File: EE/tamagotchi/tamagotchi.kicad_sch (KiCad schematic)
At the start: 0 parts

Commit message: Generic Continutation Checkin
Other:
- sheet Display ports: added GREEN_EN, RED_EN, VAPE_EN, YELLOW_EN; removed none
- sheet Power ports: added CE_N, INT_N, SCL, SDA, VSYS; removed none
- sheet Vape ports: added VAPE_EN; removed none
- note added: "TODO can 3v3 be done?"
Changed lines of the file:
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@@
 	(generator_version "9.0")
 	(paper "A4")
+	(text "TODO can 3v3 be done?"
+		(exclude_from_sim no)
+		(at 106.934 81.28 90)
+		(effects
+			(font
+				(size 1.27 1.27)
+			)
+		)
+	)
+	(wire
+		(pts
+			(xy 97.79 91.44) (xy 102.87 91.44)
+		)
+		(stroke
+			(width 0)
+			(type default)
+		)
+	)
+	(wire
+		(pts
+			(xy 102.87 91.44) (xy 102.87 87.63)
+		)
+		(stroke
+			(width 0)
+			(type default)
+		)
+	)
+	(symbol
+		(lib_id "power:+3V3")
+		(at 102.87 87.63 0)
+		(unit 1)
+		(exclude_from_sim no)
+		(in_bom yes)
+		(on_board yes)
+		(dnp no)
+		(fields_autoplaced yes)
+		(property "Reference" "#PWR09"
+			(at 102.87 91.44 0)
+			(effects
+				(font
+					(size 1.27 1.27)
+				)
+				(hide yes)
+			)
+		)
+		(property "Value" "+3V3"
+			(at 102.87 82.55 0)
+			(effects
+				(font
+					(size 1.27 1.27)
+				)
+			)
+		)
+		(property "Footprint" ""
+			(at 102.87 87.63 0)
+			(effects
+				(font
+					(size 1.27 1.27)
+				)
+				(hide yes)
+			)
+		)
+		(property "Datasheet" ""
+			(at 102.87 87.63 0)
+			(effects
+				(font
+					(size 1.27 1.27)
+				)
+				(hide yes)
+			)
+		)
+		(property "Description" "Power symbol creates a global label with name \"+3V3\""
+			(at 102.87 87.63 0)
+			(effects
+				(font
+					(size 1.27 1.27)
+				)
+				(hide yes)
+			)
+		)
+		(pin "1"
+		)
+		(instances
+			(project ""
+				(path "/47ffaef6-4682-4a87-a393-bad1a10963be"
+					(reference "#PWR09")
+					(unit 1)
+				)
+			)
+		)
+	)
 	(sheet
 		(at 52.07 88.9)
@@
 				)
 				(justify left top)
+			)
+		)
+		(pin "CE_N" input
+			(at 97.79 113.03 0)
+			(effects
+				(font
+					(size 1.27 1.27)
+				)
+				(justify right)
+			)
+		)
+		(pin "INT_N" input
+			(at 97.79 115.57 0)
+			(effects
+				(font
+					(size 1.27 1.27)
+				)
+				(justify right)
+			)
+		)
+		(pin "SCL" input
+			(at 97.79 118.11 0)
+			(effects
+				(font
+					(size 1.27 1.27)
+				)
+				(justify right)
+			)
+		)
+		(pin "SDA" input
+			(at 97.79 120.65 0)
+			(effects
+				(font
+					(size 1.27 1.27)
+				)
+				(justify right)
+			)
+		)
+		(pin "VSYS" input
+			(at 97.79 91.44 0)
+			(effects
+				(font
+					(size 1.27 1.27)
+				)
+				(justify right)
 			)
 		)
@@
 			)
 		)
+		(pin "GREEN_EN" input
+			(at 129.54 135.89 180)
+			(effects
+				(font
+					(size 1.27 1.27)
+				)
+				(justify left)
+			)
+		)
+		(pin "RED_EN" input
+			(at 129.54 138.43 180)
+			(effects
+				(font
+					(size 1.27 1.27)
+				)
+				(justify left)
+			)
+		)
+		(pin "VAPE_EN" input
+			(at 129.54 143.51 180)
+			(effects
+				(font
+					(size 1.27 1.27)
+				)
+				(justify left)
+			)
+		)
+		(pin "YELLOW_EN" input
+			(at 129.54 140.97 180)
+			(effects
+				(font
+					(size 1.27 1.27)
+				)
+				(justify left)
+			)
+		)
 		(instances
 			(project "tamagotchi"
@@
 			)
 		)
+		(pin "VAPE_EN" input
+			(at 181.61 93.98 180)
+			(effects
+				(font
+					(size 1.27 1.27)
+				)
+				(justify left)
+			)
+		)

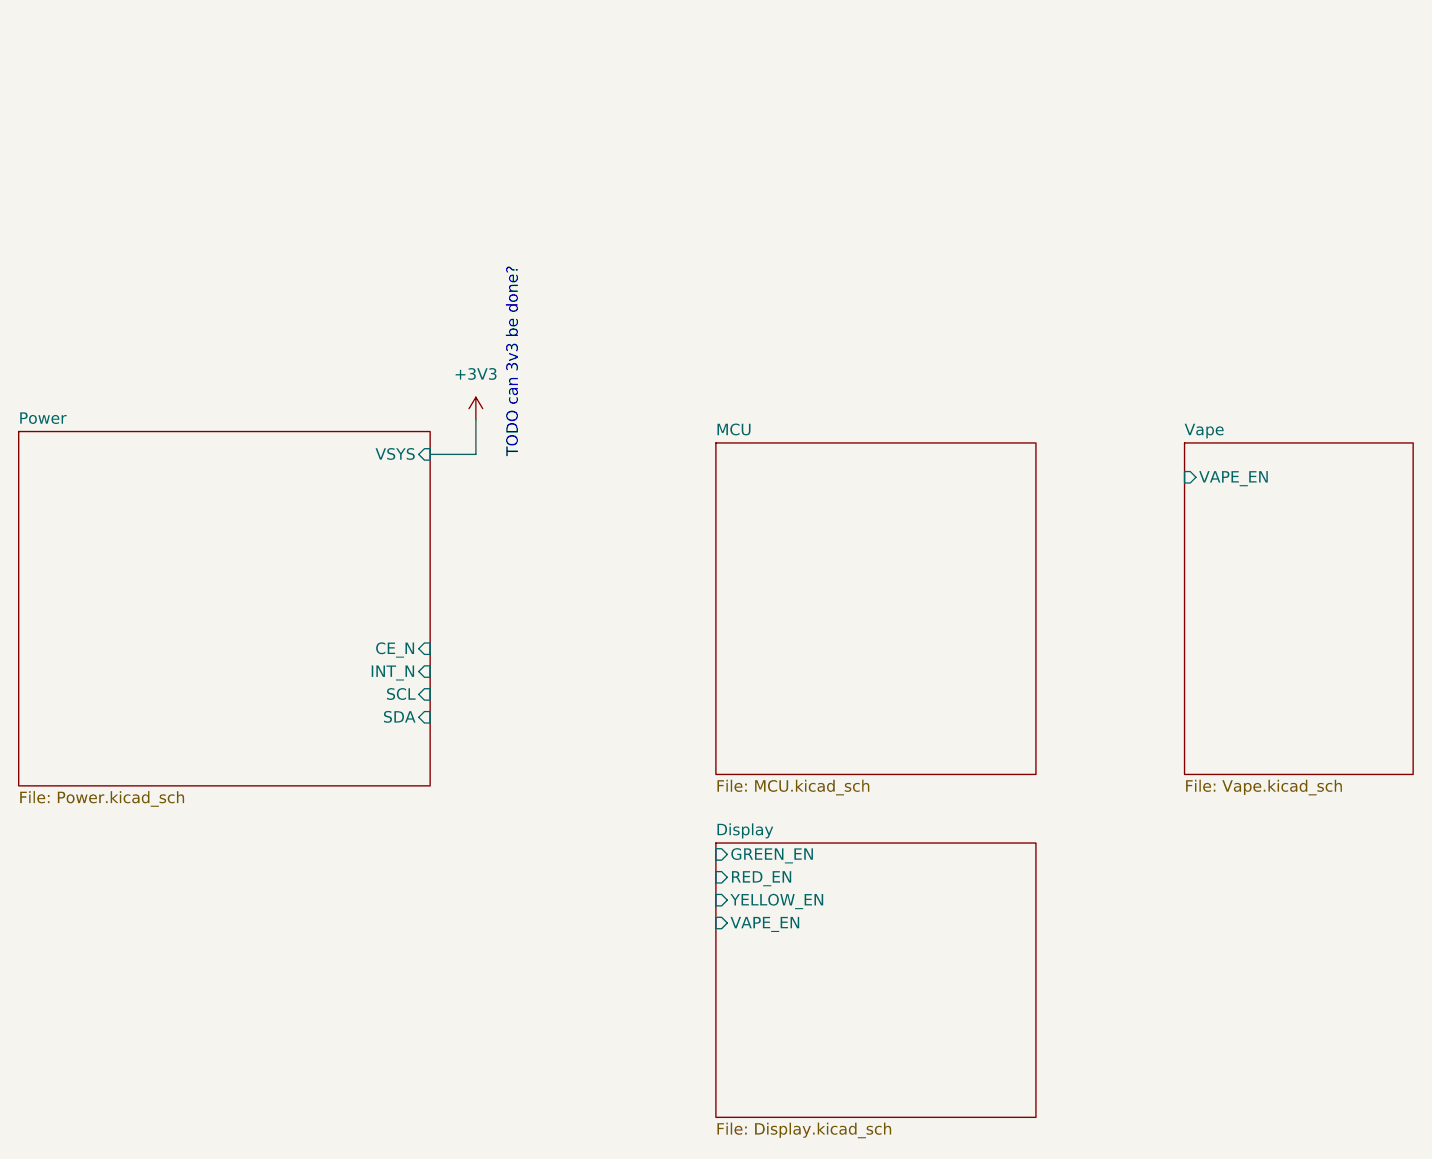
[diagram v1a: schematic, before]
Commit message: WIP - added 3D / footprints for devices. RGY LEDs aren't right
Need to do more outling / ect. super rough placement for everything.
LED footprint for RGY appears just wrong
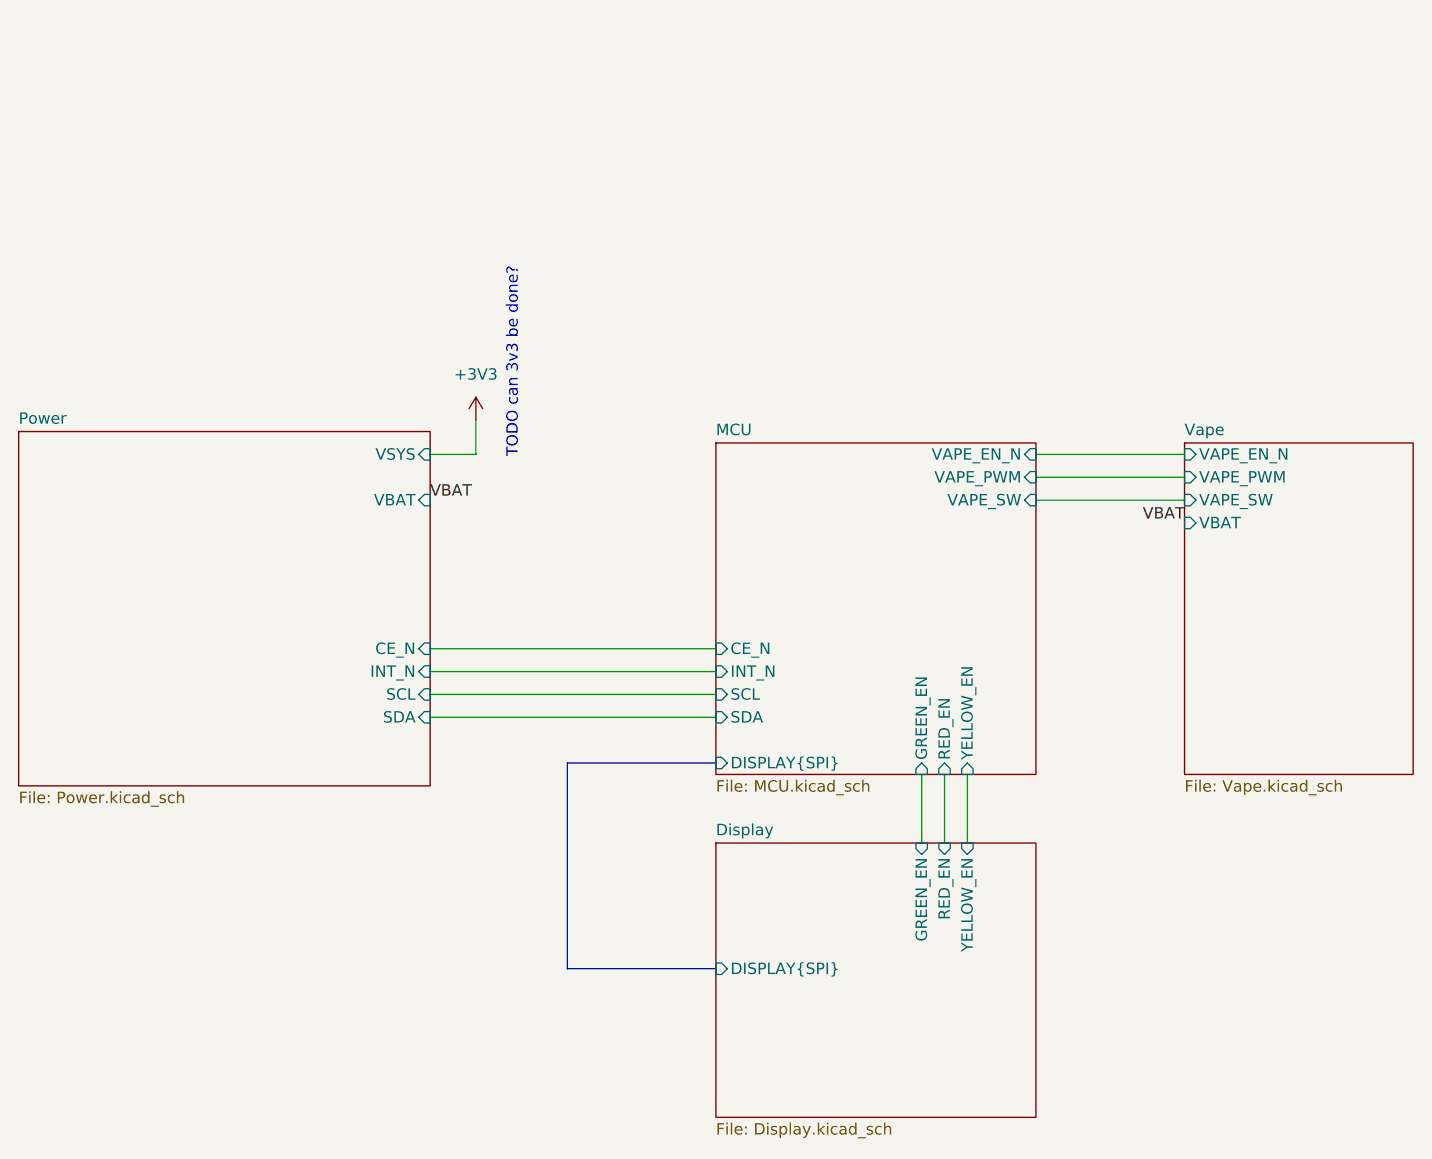
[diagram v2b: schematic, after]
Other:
- sheet Display ports: added DISPLAY{SPI}; removed VAPE_EN
- sheet MCU ports: added CE_N, DISPLAY{SPI}, GREEN_EN, INT_N, RED_EN, SCL, SDA, VAPE_EN_N, VAPE_PWM, VAPE_SW, YELLOW_EN; removed none
- sheet Power ports: added VBAT; removed none
- sheet Vape ports: added VAPE_EN_N, VAPE_PWM, VAPE_SW, VBAT; removed VAPE_EN

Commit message: Removed LEDs
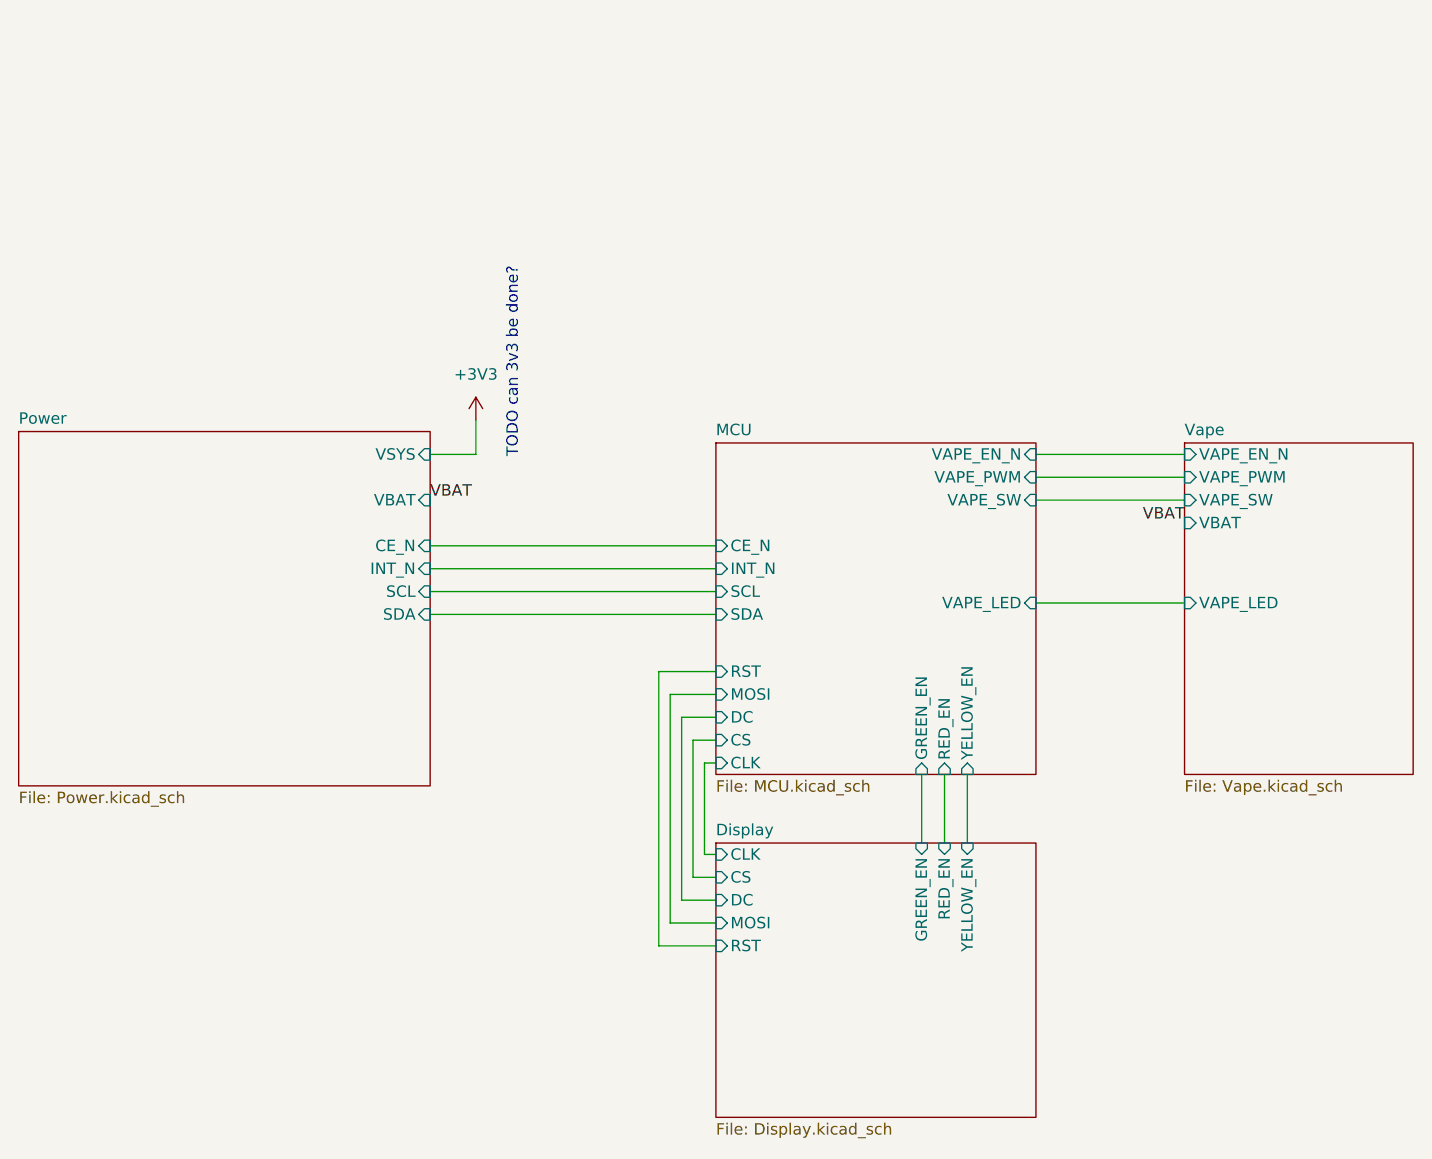
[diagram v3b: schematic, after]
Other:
- sheet Display ports: added CLK, CS, DC, MOSI, RST; removed DISPLAY{SPI}
- sheet MCU ports: added CLK, CS, DC, MOSI, RST, VAPE_LED; removed DISPLAY{SPI}
- sheet Vape ports: added VAPE_LED; removed none

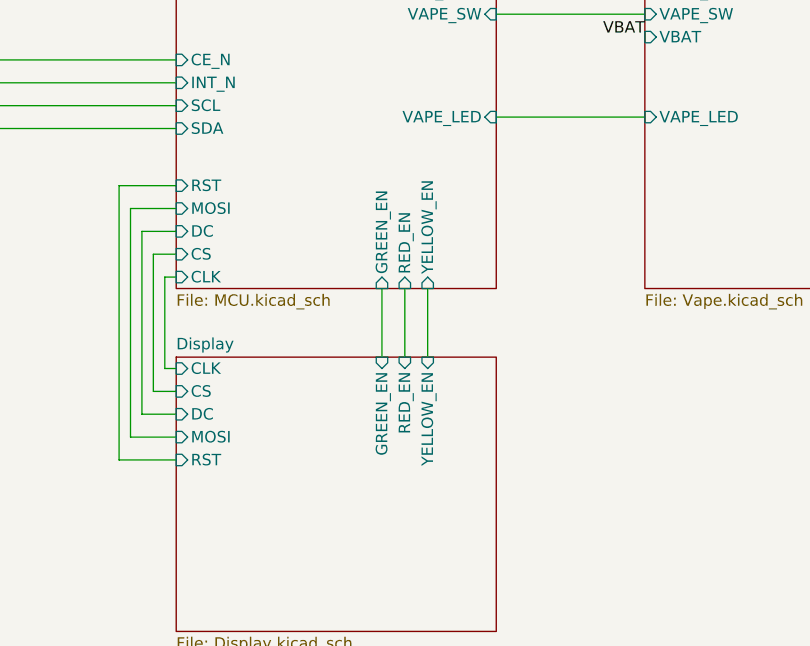
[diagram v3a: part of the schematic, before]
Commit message: First pass routing / placement & LED -> Buzzer for warning
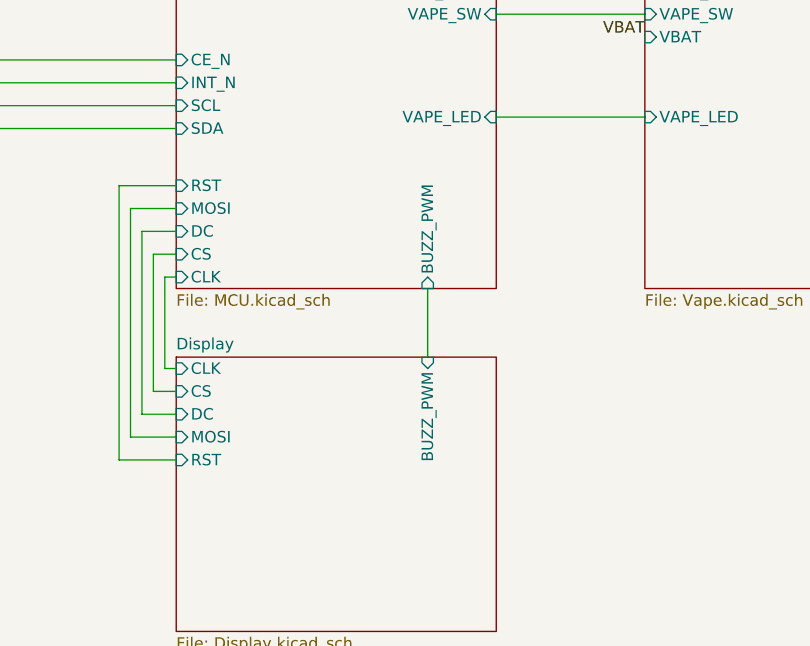
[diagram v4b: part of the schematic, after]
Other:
- sheet Display ports: added BUZZ_PWM; removed GREEN_EN, RED_EN, YELLOW_EN
- sheet MCU ports: added BUZZ_PWM; removed GREEN_EN, RED_EN, YELLOW_EN
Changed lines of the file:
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@@
+	(wire
+		(pts
+			(xy 157.48 127) (xy 157.48 134.62)
+		)
+		(stroke
+			(width 0)
+			(type default)
+		)
+	)
 	(wire
 		(pts
@@
 	(wire
 		(pts
-			(xy 152.4 127) (xy 152.4 134.62)
-		)
-		(stroke
-			(width 0)
-			(type default)
-		)
-	)
-	(wire
-		(pts
 			(xy 97.79 104.14) (xy 129.54 104.14)
 		)
@@
 	(wire
 		(pts
-			(xy 154.94 127) (xy 154.94 134.62)
-		)
-		(stroke
-			(width 0)
-			(type default)
-		)
-	)
-	(wire
-		(pts
 			(xy 165.1 107.95) (xy 181.61 107.95)
-		)
-		(stroke
-			(width 0)
-			(type default)
-		)
-	)
-	(wire
-		(pts
-			(xy 157.48 127) (xy 157.48 134.62)
 		)
 		(stroke
@@
 			)
 		)
-		(pin "GREEN_EN" input
-			(at 152.4 134.62 90)
-			(effects
-				(font
-					(size 1.27 1.27)
-				)
-				(justify right)
-			)
-		)
-		(pin "RED_EN" input
-			(at 154.94 134.62 90)
-			(effects
-				(font
-					(size 1.27 1.27)
-				)
-				(justify right)
-			)
-		)
-		(pin "YELLOW_EN" input
-			(at 157.48 134.62 90)
-			(effects
-				(font
-					(size 1.27 1.27)
-				)
-				(justify right)
-			)
-		)
 		(pin "CLK" input
 			(at 129.54 135.89 180)
@@
 				)
 				(justify left)
+			)
+		)
+		(pin "BUZZ_PWM" input
+			(at 157.48 134.62 90)
+			(effects
+				(font
+					(size 1.27 1.27)
+				)
+				(justify right)
 			)
 		)
@@
 			)
 		)
-		(pin "GREEN_EN" input
-			(at 152.4 127 270)
-			(effects
-				(font
-					(size 1.27 1.27)
-				)
-				(justify left)
-			)
-		)
 		(pin "INT_N" input
 			(at 129.54 104.14 180)
@@
 			)
 		)
-		(pin "RED_EN" input
-			(at 154.94 127 270)
-			(effects
-				(font
-					(size 1.27 1.27)
-				)
-				(justify left)
-			)
-		)
 		(pin "SCL" input
 			(at 129.54 106.68 180)
@@
 			)
 		)
-		(pin "YELLOW_EN" input
-			(at 157.48 127 270)
-			(effects
-				(font
-					(size 1.27 1.27)
-				)
-				(justify left)
-			)
-		)
 		(pin "CLK" input
 			(at 129.54 125.73 180)
@@
 			)
 		)
+		(pin "BUZZ_PWM" input
+			(at 157.48 127 270)
+			(effects
+				(font
+					(size 1.27 1.27)
+				)
+				(justify left)
+			)
+		)
